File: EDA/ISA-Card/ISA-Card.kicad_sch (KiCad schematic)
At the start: 158 parts, among them U7101 74HCT245, U7102 74HCT244, U7104 74HCT138, U7105 74HCT138, U7106 74LS08, U7107 74LS32, U7108 74LS32, U7109 74HC368, U7110 74HC04, U7111 74HC125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

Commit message: Add more schematic updates from Helen Croft
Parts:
- R10, R12, R14, R16: value R -> 270Ω
- R11, R13, R15, R9: value R -> 220Ω
- R5, R6, R7, R8: value R -> 120Ω
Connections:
- net MDB1: now also TP66.1, U7101.17 (B1), U7116.6 (QG), U7117.6 (QG), U7118.6 (QG), U7119.28 (D1); no longer TP72.1, U7101.11 (B7), U7111.3, U7116.15 (QA), U7117.15 (QA), U7118.15 (QA), U7119.8 (D7)
- net MDB2: now also TP67.1, U7101.16 (B2), U7116.5 (QF), U7117.5 (QF), U7118.5 (QF), U7119.1 (D2); no longer TP71.1, U7101.12 (B6), U7116.1 (QB), U7117.1 (QB), U7118.1 (QB), U7119.7 (D6)
- net MDB3: now also TP68.1, U7101.15 (B3), U7116.4 (QE), U7117.4 (QE), U7118.4 (QE), U7119.2 (D3); no longer TP70.1, U7101.13 (B5), U7116.2 (QC), U7117.2 (QC), U7118.2 (QC), U7119.6 (D5)
- net MDB5: now also TP70.1, U7101.13 (B5), U7116.2 (QC), U7117.2 (QC), U7118.2 (QC), U7119.6 (D5); no longer TP68.1, U7101.15 (B3), U7116.4 (QE), U7117.4 (QE), U7118.4 (QE), U7119.2 (D3)
- net MDB6: now also TP71.1, U7101.12 (B6), U7116.1 (QB), U7117.1 (QB), U7118.1 (QB), U7119.7 (D6); no longer TP67.1, U7101.16 (B2), U7116.5 (QF), U7117.5 (QF), U7118.5 (QF), U7119.1 (D2)
- net MDB7: now also TP72.1, U7101.11 (B7), U7111.3, U7116.15 (QA), U7117.15 (QA), U7118.15 (QA), U7119.8 (D7); no longer TP66.1, U7101.17 (B1), U7116.6 (QG), U7117.6 (QG), U7118.6 (QG), U7119.28 (D1)
- net MDB8 renamed MDB0
- no-connect marks 32 -> 31
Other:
- note removed: "NO IDEA"
- moved on the sheet: TP103, TP104, TP105, TP106, TP107, TP108, TP37, TP53, TP65, TP66, TP67, TP68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

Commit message: Change to correct xtal footprint
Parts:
- X-TAL1: footprint Crystal:Crystal_HC52-U_Horizontal -> Crystal:Crystal_HC49-U_Horizontal
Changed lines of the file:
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@@
     (property "Reference" "X-TAL1" (id 0) (at 252.73 21.59 0))
     (property "Value" "4.9152MHz" (id 1) (at 252.73 24.13 0))
-    (property "Footprint" "Crystal:Crystal_HC52-U_Horizontal" (id 2) (at 252.73 29.21 0)
+    (property "Footprint" "Crystal:Crystal_HC49-U_Horizontal" (id 2) (at 252.73 29.21 0)
       (effects (font (size 1.27 1.27)) hide)
     )
@@
     )
     (path "/9468e5c5-bd71-4ac5-ab4c-a5a500cbdc30"
-      (reference "X-TAL1") (unit 1) (value "4.9152MHz") (footprint "Crystal:Crystal_HC52-U_Horizontal")
+      (reference "X-TAL1") (unit 1) (value "4.9152MHz") (footprint "Crystal:Crystal_HC49-U_Horizontal")
     )
     (path "/23ebd0f7-c842-4084-92b0-885827bff78d"

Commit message: Xtal Values
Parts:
- C1, C3, C8: value C -> 100nF
- C2: value C -> 100uF
- C5, C6: value C -> 14pF
- X-TAL1: Load Capacitance (none) -> 20pf; Part Number (none) -> MP042
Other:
- note added: "12pF-16pF range"

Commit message: Final cleanup complete
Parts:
- U7104, U7105, U7109, U7116, U7117, U7118, U7120, U7121: footprint Package_DIP:DIP-16_W7.62mm -> Philips-Shapes:DIP-16-Plain
- U7106, U7107, U7108, U7110, U7111, U7112, U7113, U7114, U7115: footprint Package_DIP:DIP-14_W7.62mm -> Philips-Shapes:DIP-14-Plain

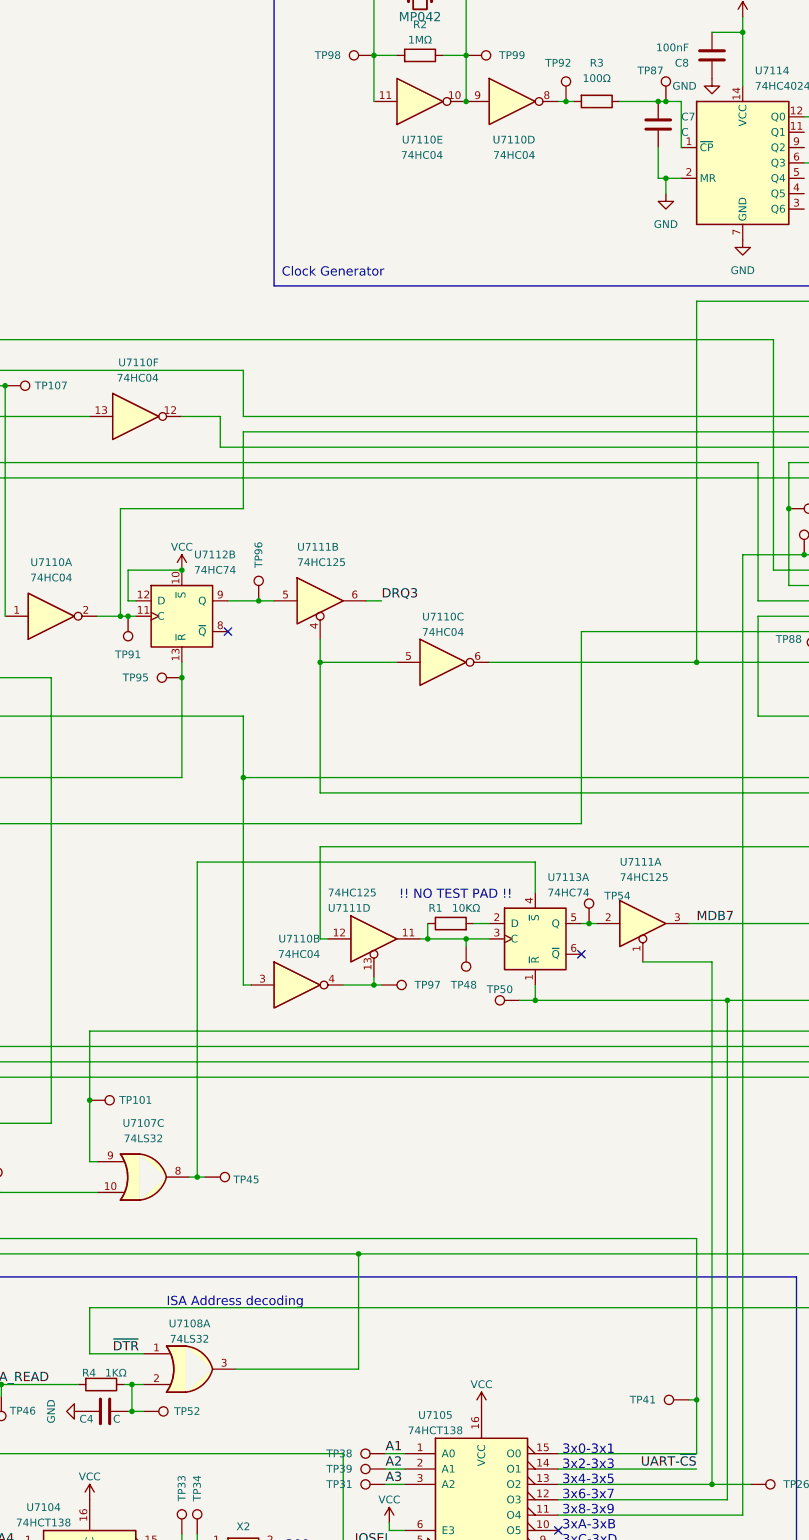
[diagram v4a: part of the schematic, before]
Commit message: Add cap values measured by Roland
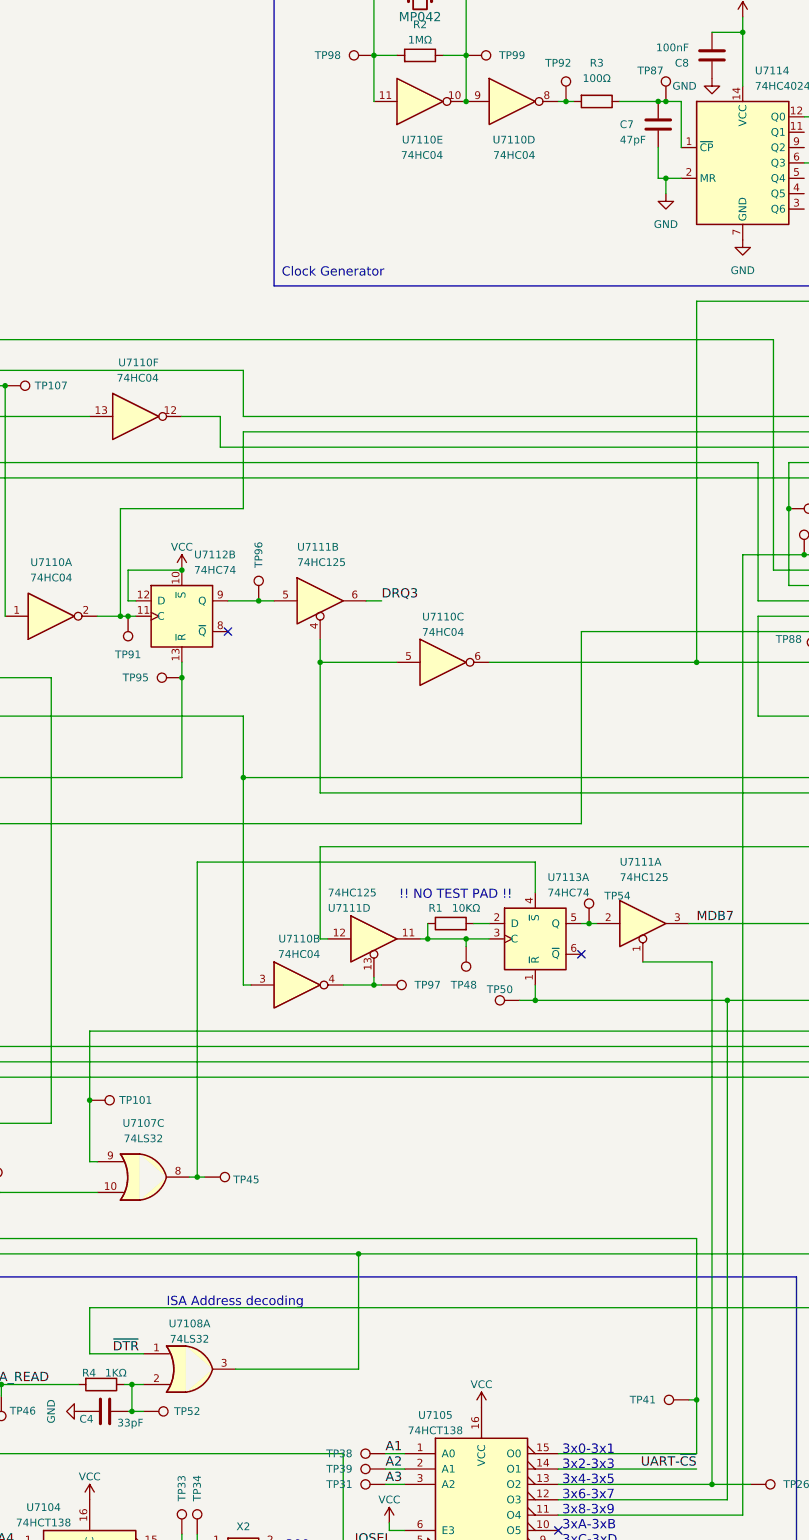
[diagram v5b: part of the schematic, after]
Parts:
- C4: value C -> 33pF
- C7: value C -> 47pF
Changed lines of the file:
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@@
   )
   (symbol (lib_id "Device:C") (at 292.1 50.8 0) (unit 1)
-    (in_bom yes) (on_board yes) (fields_autoplaced)
-    (property "Reference" "C7" (id 0) (at 295.91 49.5299 0)
-      (effects (font (size 1.27 1.27)) (justify left))
-    )
-    (property "Value" "C" (id 1) (at 295.91 52.0699 0)
+    (in_bom yes) (on_board yes)
+    (property "Reference" "C7" (id 0) (at 285.75 50.8 0)
+      (effects (font (size 1.27 1.27)) (justify left))
+    )
+    (property "Value" "47pF" (id 1) (at 285.75 53.34 0)
       (effects (font (size 1.27 1.27)) (justify left))
     )
@@
       (effects (font (size 1.27 1.27)) (justify left))
     )
-    (property "Value" "C" (id 1) (at 203.2 264.795 90)
+    (property "Value" "33pF" (id 1) (at 207.01 265.43 90)
       (effects (font (size 1.27 1.27)) (justify left))
     )
@@
     )
     (path "/d256bdaa-2cd3-48b7-98b8-d1fa7a625ded"
-      (reference "C4") (unit 1) (value "C") (footprint "Capacitor_SMD:C_1206_3216Metric")
+      (reference "C4") (unit 1) (value "33pF") (footprint "Capacitor_SMD:C_1206_3216Metric")
     )
     (path "/b66fb292-9653-482c-a3af-66a627771468"
@@
     )
     (path "/58710fde-e990-4d20-ab25-40f3807f2a2d"
-      (reference "C7") (unit 1) (value "C") (footprint "Capacitor_SMD:C_1206_3216Metric")
+      (reference "C7") (unit 1) (value "47pF") (footprint "Capacitor_SMD:C_1206_3216Metric")
     )
     (path "/8bdf772b-71bb-4b81-89e2-c4e5f9b79672"

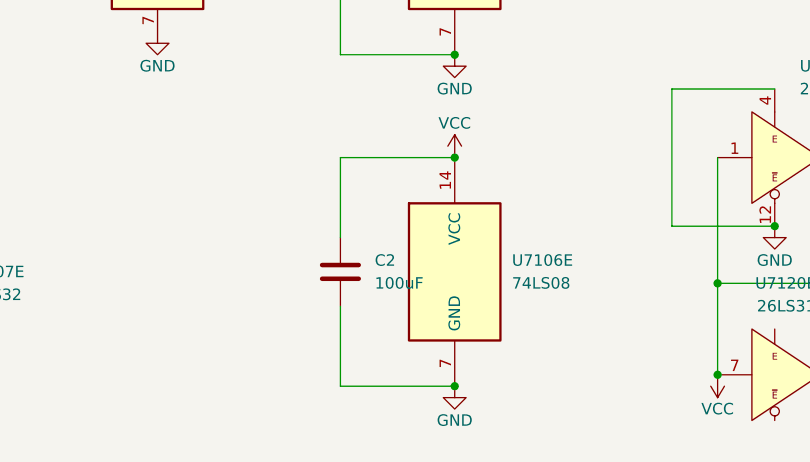
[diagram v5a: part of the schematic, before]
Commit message: Add passives (and correct C2)
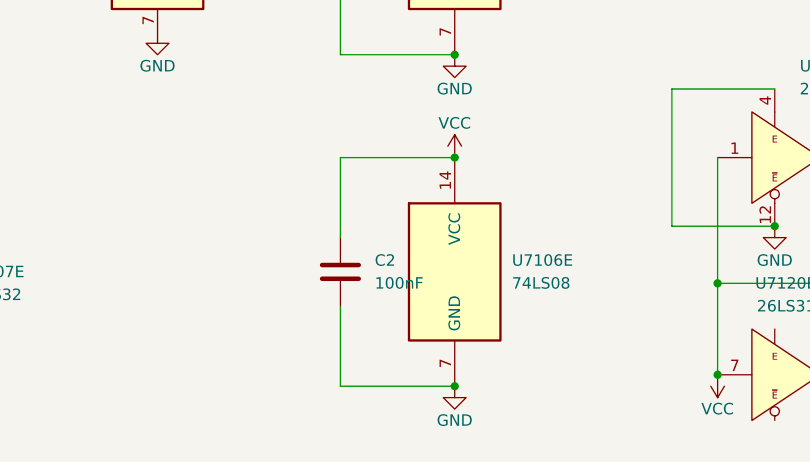
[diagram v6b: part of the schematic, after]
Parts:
- C2: value 100uF -> 100nF
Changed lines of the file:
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@@
       (effects (font (size 1.27 1.27)) (justify left))
     )
-    (property "Value" "100uF" (id 1) (at 80.01 400.0499 0)
+    (property "Value" "100nF" (id 1) (at 80.01 400.0499 0)
       (effects (font (size 1.27 1.27)) (justify left))
     )
@@
     )
     (path "/dd84c252-9d6b-4991-9b32-6677f036c621"
-      (reference "C2") (unit 1) (value "100uF") (footprint "Capacitor_SMD:C_1206_3216Metric")
+      (reference "C2") (unit 1) (value "100nF") (footprint "Capacitor_SMD:C_1206_3216Metric")
     )
     (path "/0c4d1bf0-c881-4eac-8e6b-6c518cb1e3fe"

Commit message: Attempt to group functions logically for better readability
Edited by Kicad 5, so the schematics and PCB have been upgraded
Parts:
- added unit 5 of U7120
- added unit 6 of U7120
- added unit 5 of U7121
- added unit 6 of U7121
- BUS1: symbol my_components:BUSPC_DEV -> COMM:BUSPC_DEV
- C4, C8: symbol Device:C -> Device:C_Small
- C9: symbol Device:C_Polarized -> Device:C_Polarized_Small
- U7119: symbol Z80-8251-PPI-rescue:8251 -> COMM:8251
- U7120: footprint Philips-Shapes:DIP-16-Plain -> (none); symbol Comm:26LS31 -> COMM:26LS31
- U7121: footprint Philips-Shapes:DIP-16-Plain -> (none); symbol Comm:26LS32 -> COMM:26LS32
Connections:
- net GND: now also U7120.12 (~{E}), U7120.4 (E), U7120.8 (GND), U7121.4 (E), U7121.8 (GND); no longer U7120.12, U7120.4, U7120.8 (GND), U7120.8 (GND), U7120.8 (GND), U7120.8 (GND), U7121.4, U7121.8 (GND), U7121.8 (GND), U7121.8 (GND), U7121.8 (GND)
- net VCC: now also U7120.16 (VCC), U7121.16 (VCC); no longer U7120.16 (VCC), U7120.16 (VCC), U7120.16 (VCC), U7120.16 (VCC), U7121.16 (VCC), U7121.16 (VCC), U7121.16 (VCC), U7121.16 (VCC)
- net 3XX: now reaches TP32.1, U7104.6 (E3), U7106.8
- net ISA_DCLK: now reaches TP53.1, U7105.11 (O4), U7109.2 (I1)
- net ATTN_RD: now reaches TP50.1, U7105.12 (O3), U7113.1 (~{R}), U7118.13 (~{OE})
- net ~{CMD_DONE}: now reaches TP26.1, U7105.13 (O2), U7111.1
- net ~{LOAD_CMD}: now reaches TP41.1, U7105.15 (O0), U7106.12, U7109.14 (I6), U7112.1 (~{R}), U7113.10 (~{S})
- net ~{ATTN_RDY}: now reaches TP104.1, U7110.13, U7115.4 (Q5)
- net ~{DMA_DTR}: now reaches TP93.1, U7106.2, U7108.10, U7108.12, U7108.3, U7112.3 (C)
- net DATA_RDY: now reaches TP91.1, U7110.2, U7112.11 (C), U7116.12 (RCLK), U7117.12 (RCLK)
- net ATTN_RDY: now reaches TP57.1, U7110.12, U7111.12, U7118.12 (RCLK)
- net ~{ISA_CTL}: now reaches TP88.1, U7109.1 (OEa), U7110.6, U7111.10
- net ATTN_SMP: now reaches TP106.1, U7115.9 (Q2), U7118.11 (SRCLK)
- net T_ATTN: now reaches TP103.1, U7109.10 (I4), U7115.3 (Q6)
- net ATTNb: now reaches TP101.1, U7107.9, U7109.11 (O5b)
- net ~{LOAD_CMD_DLY}: now reaches TP105.1, U7109.13 (O6b), U7115.2 (MR)
- net T_DATA: now reaches TP108.1, U7109.4 (I2), U7115.12 (Q0)
- net ~{DATA_RDY}: now reaches TP107.1, U7110.1, U7115.6 (Q3)
- net RTS: now reaches TP97.1, U7110.4, U7111.13
- net ~{DMA_RD}: now reaches C4.2, R4.1, TP52.1, U7108.2
- net Attention renamed ATTN
- net CLKp0 renamed CLKP0
- net CLKp3 renamed CLKP3
- net Command renamed CMD
- net DMA_ACK: no longer names the net of TP43.1, U7102.14 (1Y2), U7108.5
- net DMA_READ: no longer names the net of R4.2, TP46.1, U7108.6
- net Data renamed DATA
- net Data Clock renamed DCLK
- net IOACT renamed ~{IO_ACT}
- net IOSEL renamed ~{IO_SEL}
- net M1: no longer names the net of X3.6
- net M2: no longer names the net of X3.14 (P14)
- net M3: no longer names the net of X3.7
- net M4: no longer names the net of X3.15 (P15)
- net RXD renamed RESP
- net U7116-~{OE}: no longer names the net of TP102.1, U7108.8, U7116.13 (~{OE})
- net U7117-~{OE}: no longer names the net of TP37.1, U7108.11, U7117.13 (~{OE})
- net ~{DTR} renamed ~{CD_CTL}
- net ~{CD_CTL}: now also U7121.12 (~{E}); no longer U7121.12
- no-connect marks 31 -> 77
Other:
- note added: "8251 Clock Generator"
- note added: "CD Interface"
- note added: "Data Input"
- note added: "ISA Address/control buffer"
- note added: "ISA Control Transceiver"
- note added: "Sequencer"
- note removed: "Clock Generator"
- note removed: "Drive Interfacing"
- note removed: "ISA Address/controll buffer"
- note removed: "VERY WRONG"
- moved on the sheet: C2, C3, C4, C5, C6, C7, C8, C9, R1, R10, R11, R12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

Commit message: Tweaks to the schematic
Added explanation of circuit to project description
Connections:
- net ATTNb renamed ~{ATTN}
- net DCLK renamed ~{DCLK}
- net ISA_DCLK renamed ~{ISA_DCLK}
- net ~{LOAD_CMD_DLY} renamed DATA_RST
- net ~{LOAD_CMD} renamed ~{DATA_RST}
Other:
- note added: "Status Input"
- moved on the sheet: TP26, TP31, TP38, TP39, TP41, TP50, TP53, TP54, TP81, TP84, TP88, TP91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
